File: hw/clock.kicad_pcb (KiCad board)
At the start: 2 copper layers, 109.9 x 52.5 mm, 73 parts, among them J1 USB-A1HSW6, J2 USB-A1HSW6, J3 USB-A1HSW6, SW1 TL3305AF260QG, SW2 TL3305AF260QG, SW3 TL3305AF260QG, U1 LPC812M101JDH20, U10 HDSP-5321 Common Anode, U11 HDSP-5321 Common Anode, U12 HDSP-5321 Common Anode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

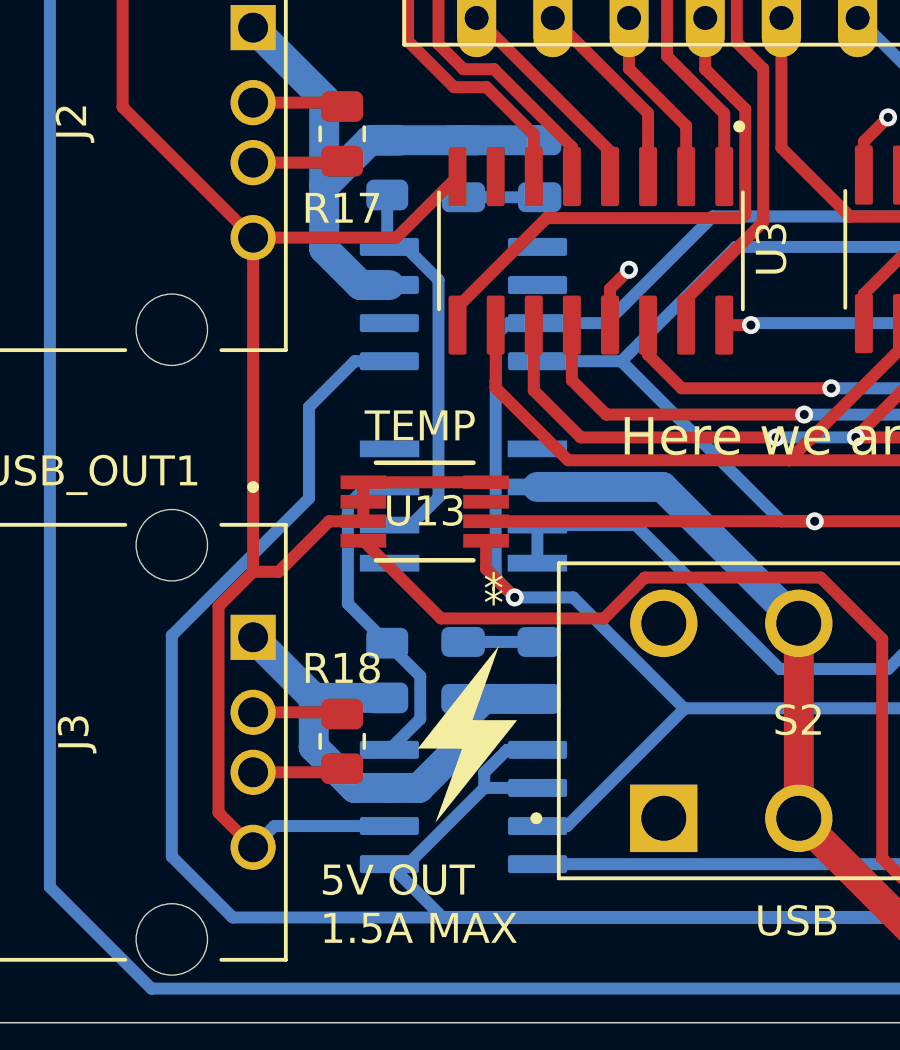
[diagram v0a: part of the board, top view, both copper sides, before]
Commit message: Increase usb out trace widths
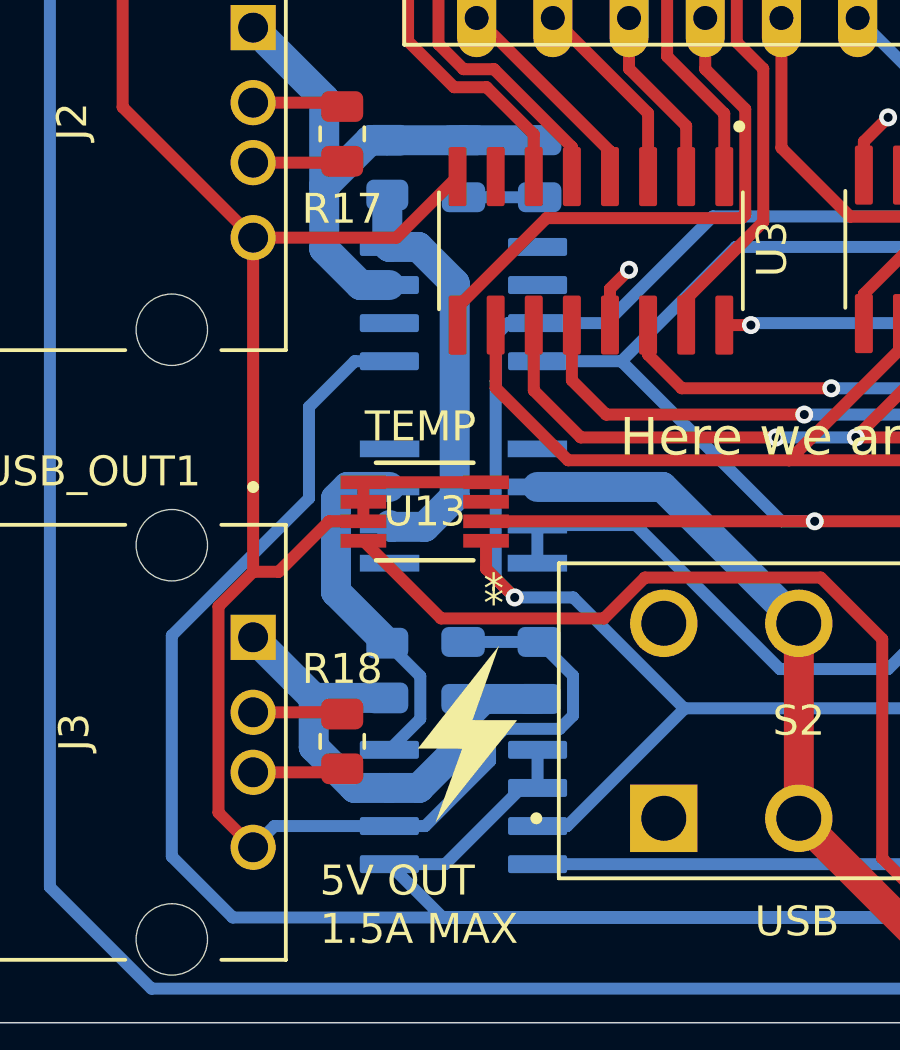
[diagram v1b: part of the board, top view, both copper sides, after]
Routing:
- net GND: track 174.6 -> 185.5 mm
- net CURR_SENS_2: track 13.5 -> 15.1 mm
- net CURR_SENS_1: track 11.2 -> 12.7 mm
- net +3V3: track 359.1 -> 357.8 mm
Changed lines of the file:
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@@
 	)
 	(segment
-		(start 154.572 95.504)
-		(end 155.194 95.504)
+		(start 156.43317 95.504)
+		(end 154.572 95.504)
 		(width 0.4)
 		(layer "B.Cu")
@@
 	)
 	(segment
-		(start 158.496 91.694)
-		(end 157.734 92.456)
-		(width 0.4)
-		(layer "B.Cu")
-		(net 6)
-	)
-	(segment
 		(start 151.892 83.312)
 		(end 151.892 80.264)
@@
 	)
 	(segment
+		(start 158.97317 92.964)
+		(end 156.43317 95.504)
+		(width 0.4)
+		(layer "B.Cu")
+		(net 6)
+	)
+	(segment
 		(start 211.5155 92.548)
 		(end 212.4105 92.548)
@@
 	)
 	(segment
-		(start 155.194 95.504)
-		(end 157.734 92.964)
-		(width 0.4)
-		(layer "B.Cu")
-		(net 6)
-	)
-	(segment
 		(start 222.551219 77.535)
 		(end 235.304333 77.535)
@@
 	)
 	(segment
-		(start 157.734 92.456)
-		(end 157.734 92.964)
-		(width 0.4)
-		(layer "B.Cu")
-		(net 6)
-	)
-	(segment
 		(start 172.974 97.282)
 		(end 149.352 97.282)
@@
 	)
 	(segment
+		(start 159.512 91.694)
+		(end 159.512 92.964)
+		(width 0.4)
+		(layer "B.Cu")
+		(net 6)
+	)
+	(segment
 		(start 179.81 57.785)
 		(end 179.01 57.785)
@@
 	)
 	(segment
+		(start 159.512 92.964)
+		(end 158.97317 92.964)
+		(width 0.4)
+		(layer "B.Cu")
+		(net 6)
+	)
+	(segment
 		(start 182.118 60.093)
 		(end 179.81 57.785)
@@
 	)
 	(segment
-		(start 159.512 91.694)
-		(end 158.496 91.694)
-		(width 0.4)
-		(layer "B.Cu")
-		(net 6)
-	)
-	(segment
-		(start 157.734 92.964)
-		(end 159.512 92.964)
-		(width 0.4)
-		(layer "B.Cu")
-		(net 6)
-	)
-	(segment
 		(start 233.172 81.28)
 		(end 233.172 82.16505)
@@
 	)
 	(segment
-		(start 153.1876 86.8236)
-		(end 153.1876 83.5404)
-		(width 0.4)
+		(start 154.502 88.138)
+		(end 152.792 86.428)
+		(width 1)
 		(layer "B.Cu")
 		(net 28)
@@
 	)
 	(segment
-		(start 153.1876 83.5404)
-		(end 153.797 82.931)
-		(width 0.4)
-		(layer "B.Cu")
-		(net 28)
-	)
-	(segment
-		(start 154.502 88.138)
-		(end 153.1876 86.8236)
-		(width 0.4)
-		(layer "B.Cu")
-		(net 28)
-	)
-	(segment
 		(start 155.602 89.238)
 		(end 154.502 88.138)
@@
 	)
 	(segment
+		(start 152.792 86.428)
+		(end 152.792 83.3172)
+		(width 1)
+		(layer "B.Cu")
+		(net 28)
+	)
+	(segment
+		(start 153.1782 82.931)
+		(end 154.5782 82.931)
+		(width 1)
+		(layer "B.Cu")
+		(net 28)
+	)
+	(segment
+		(start 152.792 83.3172)
+		(end 153.1782 82.931)
+		(width 1)
+		(layer "B.Cu")
+		(net 28)
+	)
+	(segment
 		(start 155.602 90.664)
 		(end 155.602 89.238)
@@
 	)
 	(segment
-		(start 155.2894 84.201)
-		(end 156.21 83.2804)
-		(width 0.4)
+		(start 155.75 84.2604)
+		(end 156.75 83.2604)
+		(width 1)
+		(layer "B.Cu")
+		(net 29)
+	)
+	(segment
+		(start 154.6376 84.2604)
+		(end 155.75 84.2604)
+		(width 1)
 		(layer "B.Cu")
 		(net 29)
@@
 		(start 154.502 74.86)
 		(end 154.572 74.93)
-		(width 0.4)
+		(width 1)
 		(layer "B.Cu")
 		(net 29)
 	)
 	(segment
-		(start 156.21 76.02917)
-		(end 155.11083 74.93)
-		(width 0.4)
+		(start 156.75 76.144906)
+		(end 155.535094 74.93)
+		(width 1)
 		(layer "B.Cu")
 		(net 29)
 	)
 	(segment
-		(start 154.5782 84.201)
-		(end 155.2894 84.201)
-		(width 0.4)
-		(layer "B.Cu")
-		(net 29)
-	)
-	(segment
-		(start 156.21 83.2804)
-		(end 156.21 76.02917)
-		(width 0.4)
+		(start 156.75 83.2604)
+		(end 156.75 76.144906)
+		(width 1)
 		(layer "B.Cu")
 		(net 29)
@@
 		(start 154.502 73.199)
 		(end 154.502 74.86)
-		(width 0.4)
+		(width 1)
+		(layer "B.Cu")
+		(net 29)
+	)
+	(segment
+		(start 155.535094 74.93)
+		(end 154.572 74.93)
+		(width 1)
 		(layer "B.Cu")
 		(net 29)
@@
 	)
 	(segment
+		(start 154.5782 84.201)
+		(end 154.6376 84.2604)
+		(width 1)
+		(layer "B.Cu")
+		(net 29)
+	)
+	(segment
 		(start 154.131 73.199)
 		(end 154.502 73.199)
@@
 	)
 	(segment
+		(start 155.766 94.234)
+		(end 154.572 94.234)
+		(width 0.4)
+		(layer "B.Cu")
+		(net 30)
+	)
+	(segment
 		(start 212.9155 86.8045)
 		(end 213.36 86.36)
@@
 	)
 	(segment
+		(start 160.25 90.994)
+		(end 158.40317 90.994)
+		(width 0.4)
+		(layer "B.Cu")
+		(net 30)
+	)
+	(segment
+		(start 160.693422 89.221812)
+		(end 160.693422 90.550578)
+		(width 0.4)
+		(layer "B.Cu")
+		(net 30)
+	)
+	(segment
 		(start 212.2805 94.107)
 		(end 212.2805 94.947472)
@@
 	)
 	(segment
+		(start 159.568422 88.096812)
+		(end 160.693422 89.221812)
+		(width 0.4)
+		(layer "B.Cu")
+		(net 30)
+	)
+	(segment
 		(start 157.042 73.274)
 		(end 159.582 73.274)
@@
 	)
 	(segment
+		(start 158.40317 90.994)
+		(end 157.928422 91.468748)
+		(width 0.4)
+		(layer "B.Cu")
+		(net 30)
+	)
+	(segment
 		(start 159.582 74.86)
 		(end 159.512 74.93)
@@
 		(width 0.4)
 		(layer "B.Cu")
+		(net 30)
+	)
+	(segment
+		(start 157.928422 92.071578)
+		(end 155.766 94.234)
+		(width 0.4)
+		(layer "B.Cu")
+		(net 30)
+	)
+	(segment
+		(start 157.928422 91.468748)
+		(end 157.928422 92.071578)
+		(width 0.4)
+		(layer "B.Cu")
+		(net 30)
+	)
+	(segment
+		(start 160.693422 90.550578)
+		(end 160.25 90.994)
+		(width 0.4)
+		(layer "B.Cu")

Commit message: Change passives
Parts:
- C1, C2: value 18pf -> 16pf
- C13: value 10nf -> 1uf
- C3, C4: value 12.5pf -> 19pf
- C5, C8, C9: value 120uf -> 100uf
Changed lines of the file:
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@@
 			)
 		)
-		(property "Value" "18pf"
+		(property "Value" "16pf"
 			(at 0 1.68 90)
 			(layer "F.Fab")
@@
 			)
 		)
-		(property "Value" "18pf"
+		(property "Value" "16pf"
 			(at 0 1.68 90)
 			(layer "F.Fab")
@@
 			)
 		)
-		(property "Value" "120uf"
+		(property "Value" "100uf"
 			(at 0 1.68 90)
 			(layer "F.Fab")
@@
 			)
 		)
-		(property "Value" "10nf"
+		(property "Value" "1uf"
 			(at 0 1.68 0)
 			(layer "F.Fab")
@@
 			)
 		)
-		(property "Value" "120uf"
+		(property "Value" "100uf"
 			(at 0 -1.68 90)
 			(layer "B.Fab")
@@
 			)
 		)
-		(property "Value" "12.5pf"
+		(property "Value" "19pf"
 			(at 0 -1.68 0)
 			(layer "B.Fab")
@@
 			)
 		)
-		(property "Value" "120uf"
+		(property "Value" "100uf"
 			(at 0 -1.68 90)
 			(layer "B.Fab")
@@
 			)
 		)
-		(property "Value" "12.5pf"
+		(property "Value" "19pf"
 			(at 0 -1.68 0)
 			(layer "B.Fab")
